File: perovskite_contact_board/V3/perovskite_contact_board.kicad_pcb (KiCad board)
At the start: 2 copper layers, 55.2 x 55.2 mm, 31 parts, among them U1 Perovskite_CP_6_Cell, U2 Perovskite_CP_6_Cell, U3 Perovskite_CP_6_Cell, U4 MCP9808_MSOP, U5 MCP9808_MSOP, U6 MCP9808_MSOP

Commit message: Review contact board
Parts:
- moved JP100.7 52.8 mm to (159.3, 98.7)
- moved JP101.3 52.8 mm to (143.8, 115.4)
- moved JP101.4 52.8 mm to (143.8, 125.1)
- moved JP102.2 52.8 mm to (171.7, 115.2)
- moved JP102.4 52.8 mm to (170.2, 125.1)
- moved JP102.6 52.8 mm to (163.1, 125.1)
- moved JP103.1 52.8 mm to (160.0, 89.5)
- moved JP103.2 52.8 mm to (158.5, 115.2)
- moved U4 52.8 mm to (166.4, 94.2)
- moved U5 52.8 mm to (140.3, 120.4)
- moved U6 52.8 mm to (166.4, 120.3)
- moved JP100.1 52.8 mm to (163.3, 89.5)
- moved JP100.2 52.8 mm to (166.6, 89.5)
- moved JP100.5 52.8 mm to (166.6, 98.7)
- moved JP100.6 52.8 mm to (163.3, 98.7)
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
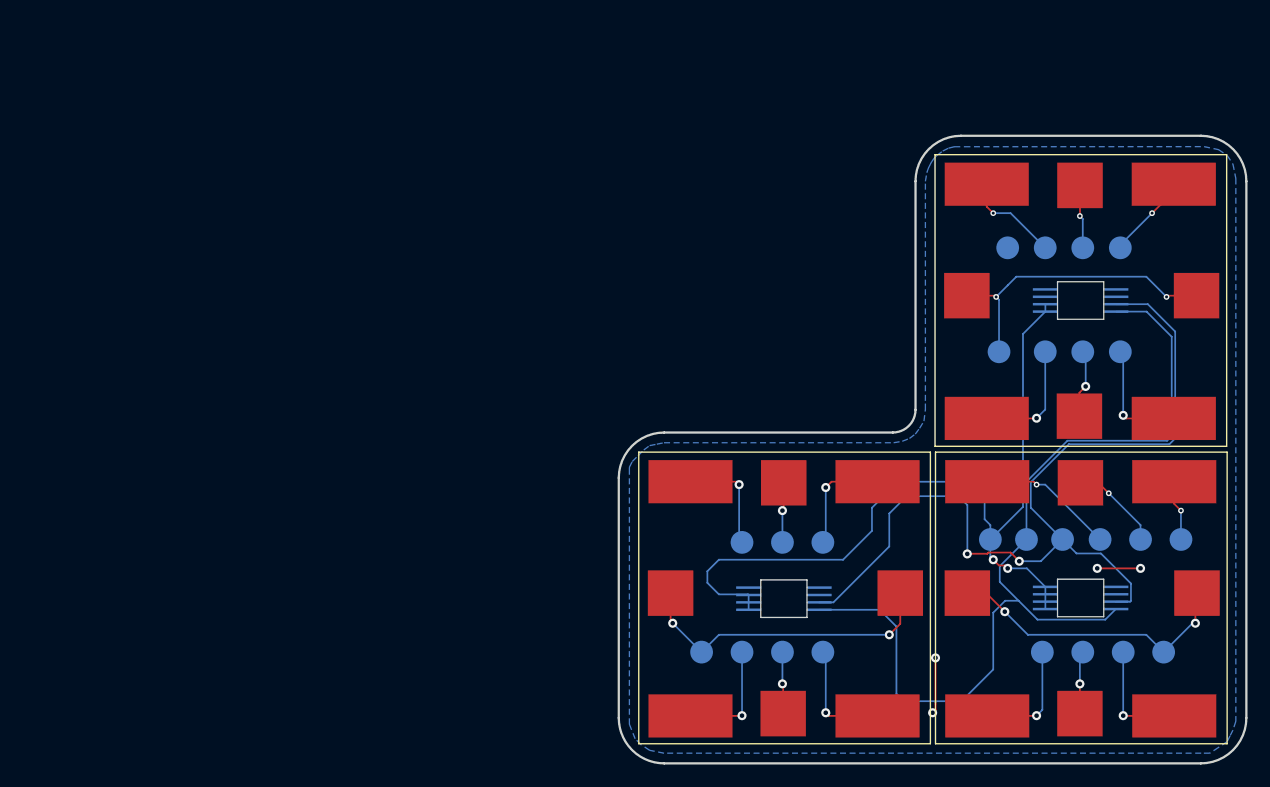
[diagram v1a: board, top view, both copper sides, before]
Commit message: centered vias, added all redundant pads, standardized text
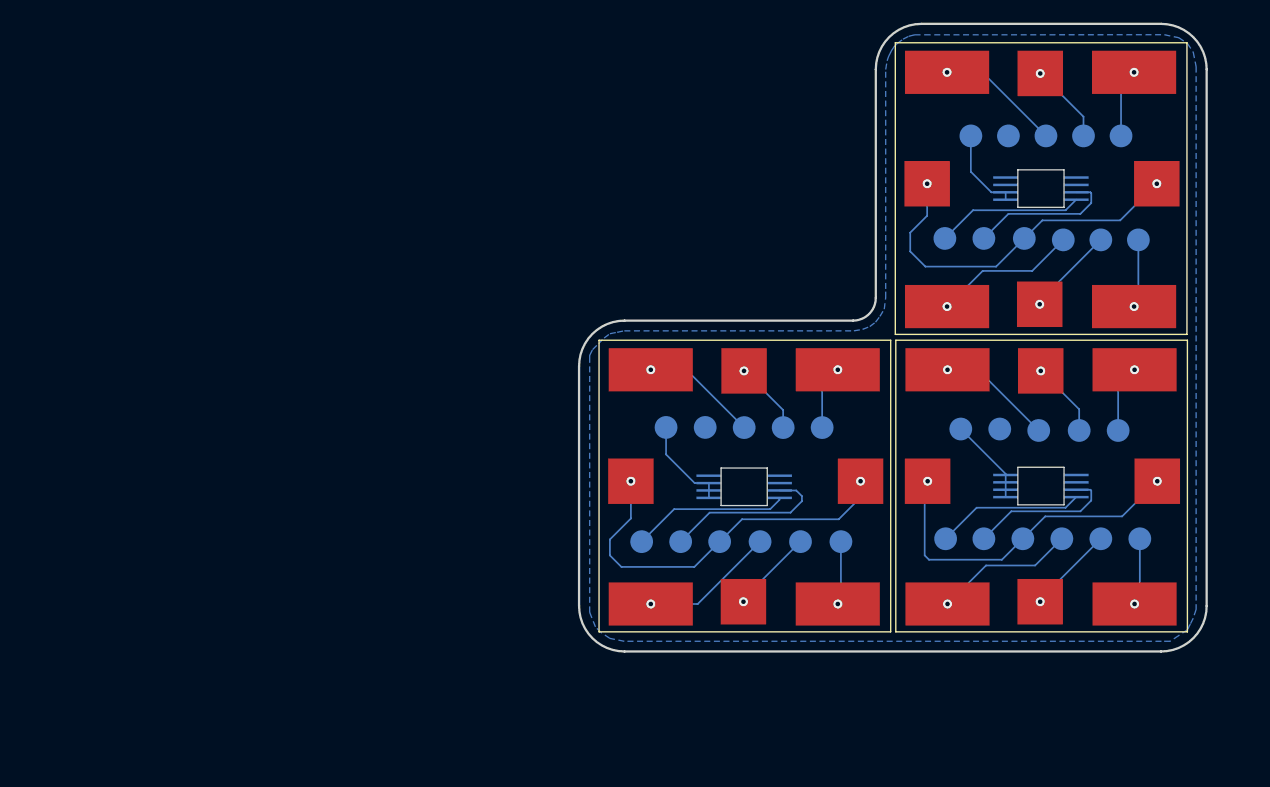
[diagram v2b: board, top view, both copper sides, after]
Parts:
- added JP103.10: Conn_01x01, TestPoint:TestPoint_Pad_D2.0mm, B.Cu at (155.9, 105.5)
- added JP103.11: Conn_01x01, TestPoint:TestPoint_Pad_D2.0mm, B.Cu at (157.9, 115.1)
- added JP103.12: Conn_01x01, TestPoint:TestPoint_Pad_D2.0mm, B.Cu at (154.6, 115.1)
- added JP103.5: Conn_01x01, TestPoint:TestPoint_Pad_D2.0mm, B.Cu at (133.4, 105.3)
- added JP103.6: Conn_01x01, TestPoint:TestPoint_Pad_D2.0mm, B.Cu at (130.0, 105.3)
- added JP103.7: Conn_01x01, TestPoint:TestPoint_Pad_D2.0mm, B.Cu at (131.3, 115.4)
- added JP103.8: Conn_01x01, TestPoint:TestPoint_Pad_D2.0mm, B.Cu at (127.8, 115.4)
- added JP103.9: Conn_01x01, TestPoint:TestPoint_Pad_D2.0mm, B.Cu at (159.3, 105.5)
- moved JP103.2 35.5 mm to (156.8, 79.7), turned to 180 degrees
- moved JP103.4 27.4 mm to (154.5, 88.7)
- moved JP103.3 27.4 mm to (157.9, 88.7)
- moved JP102.7 15.9 mm to (161.4, 115.1)
- moved JP102.3 11.1 mm to (169.7, 105.6)
- moved JP102.1 11.0 mm to (162.8, 105.6)
- moved JP102.2 11.0 mm to (166.3, 105.6)
- moved U1 10.4 mm to (150.1, 71.5)
- moved U2 10.4 mm to (124.1, 97.7)
- moved U4 10.4 mm to (162.9, 84.3)
- moved U5 10.4 mm to (136.8, 110.6)
- moved U6 10.4 mm to (162.9, 110.5)
- moved U3 10.4 mm to (150.2, 97.7)
- moved JP100.7 10.2 mm to (161.5, 88.7)
- moved JP102.6 10.1 mm to (164.8, 115.1)
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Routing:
- net VDD: track 71.7 -> 23.7 mm, vias 2 -> 0
- net SDA: track 81.7 -> 39.8 mm
- net SCL: track 79.4 -> 40.8 mm, vias 2 -> 0
- net GND: track 8.74 -> 0.00 mm, vias 4 -> 0
- net CP_2: track 27.5 -> 33.7 mm
- net CP_1: track 26.7 -> 31.8 mm
- net CELL_10: track 10.1 -> 5.60 mm
- net CELL_4: track 10.3 -> 6.02 mm
- net CP_3: track 26.0 -> 30.1 mm
- net CELL_9: track 9.70 -> 5.65 mm
- net CELL_16: track 10.1 -> 6.11 mm
- net CELL_1: track 8.61 -> 11.0 mm
- net CELL_18: track 10.1 -> 12.4 mm
- net CELL_17: track 5.52 -> 7.75 mm
- net CELL_6: track 10.5 -> 12.7 mm
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
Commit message: isolating nets and fixing silk screen
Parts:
- moved JP103.9 0.14 mm to (159.3, 105.6)
- moved JP103.10 0.13 mm to (155.9, 105.6)
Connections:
- JP103.10 pad 1: VDD -> VDDF
- JP103.11 pad 1: SCL -> SCL3
- JP103.12 pad 1: SDA -> SDA3
- JP103.3 pad 1: SCL -> SCL1
- JP103.4 pad 1: SDA -> SDA1
- JP103.6 pad 1: VDD -> VDDA
- JP103.7 pad 1: SCL -> SCL2
- JP103.8 pad 1: SDA -> SDA2
- U4 pad 1: SDA -> SDA1
- U4 pad 2: SCL -> SCL1
- U5 pad 1: SDA -> SDA2
- U5 pad 2: SCL -> SCL2
- U5 pad 6: VDD -> VDDA
- U5 pad 7: VDD -> VDDA
- U5 pad 8: VDD -> VDDA
- U6 pad 1: SDA -> SDA3
- U6 pad 2: SCL -> SCL3
- U6 pad 5: VDD -> VDDF
- U6 pad 6: VDD -> VDDF
- U6 pad 7: VDD -> VDDF
- U6 pad 8: VDD -> VDDF
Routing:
- net SCL: track 40.8 -> 0.00 mm
- net SDA: track 39.8 -> 0.00 mm
- net VDD: track 23.7 -> 7.61 mm
- net SCL2: track 0.00 -> 14.8 mm
- net SDA2: track 0.00 -> 13.8 mm
- net SCL3: track 0.00 -> 13.1 mm
- net SDA3: track 0.00 -> 13.0 mm
- net SCL1: track 0.00 -> 13.0 mm
- net SDA1: track 0.00 -> 13.0 mm
- net VDDA: track 0.00 -> 8.49 mm
- net VDDF: track 0.00 -> 7.52 mm

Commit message: Approve V3 of perovskite contact board
- Generate gerbers
- Generate renders
- Update copyright year and approved line
- Add NREL tester board firmware
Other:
- board text added: "*"
